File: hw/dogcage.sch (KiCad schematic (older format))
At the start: 23 parts, among them CON1 BARREL_JACK, P1 Door, P2 Lock, Q1 TIP120, Q2 TIP120, SW1 SW_PUSH, SW2 SW_PUSH, U1 LD1117S50TR, U2 ESP-01v090, U3 LD1117S33TR, U4 TEENSYLC

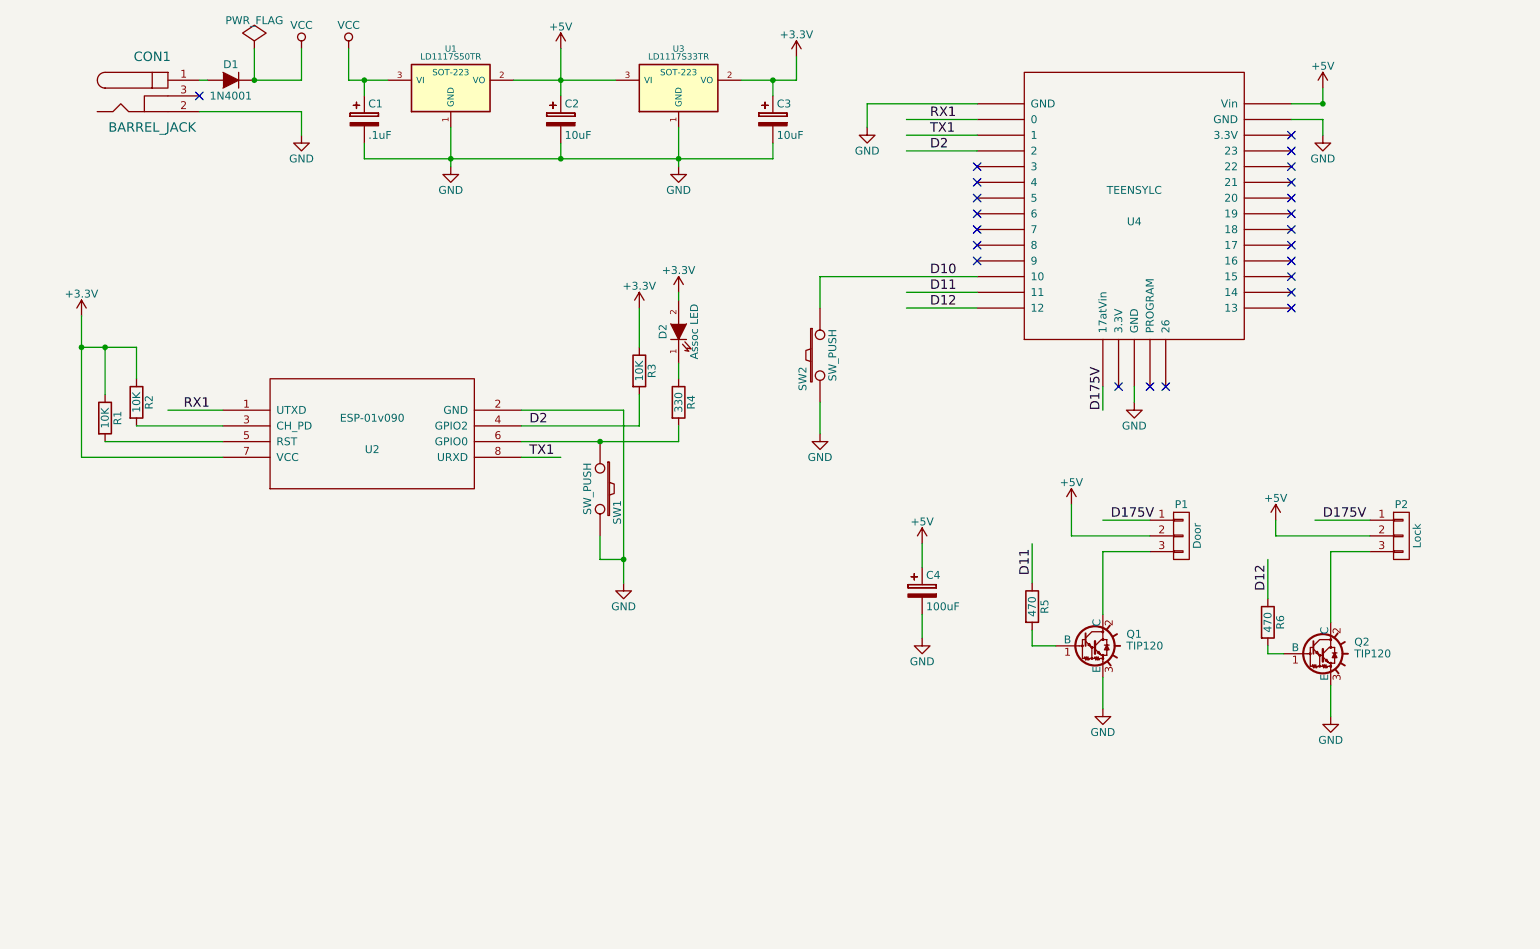
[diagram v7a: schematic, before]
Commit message: Added pwr_flag to GND, fixed DRC failures
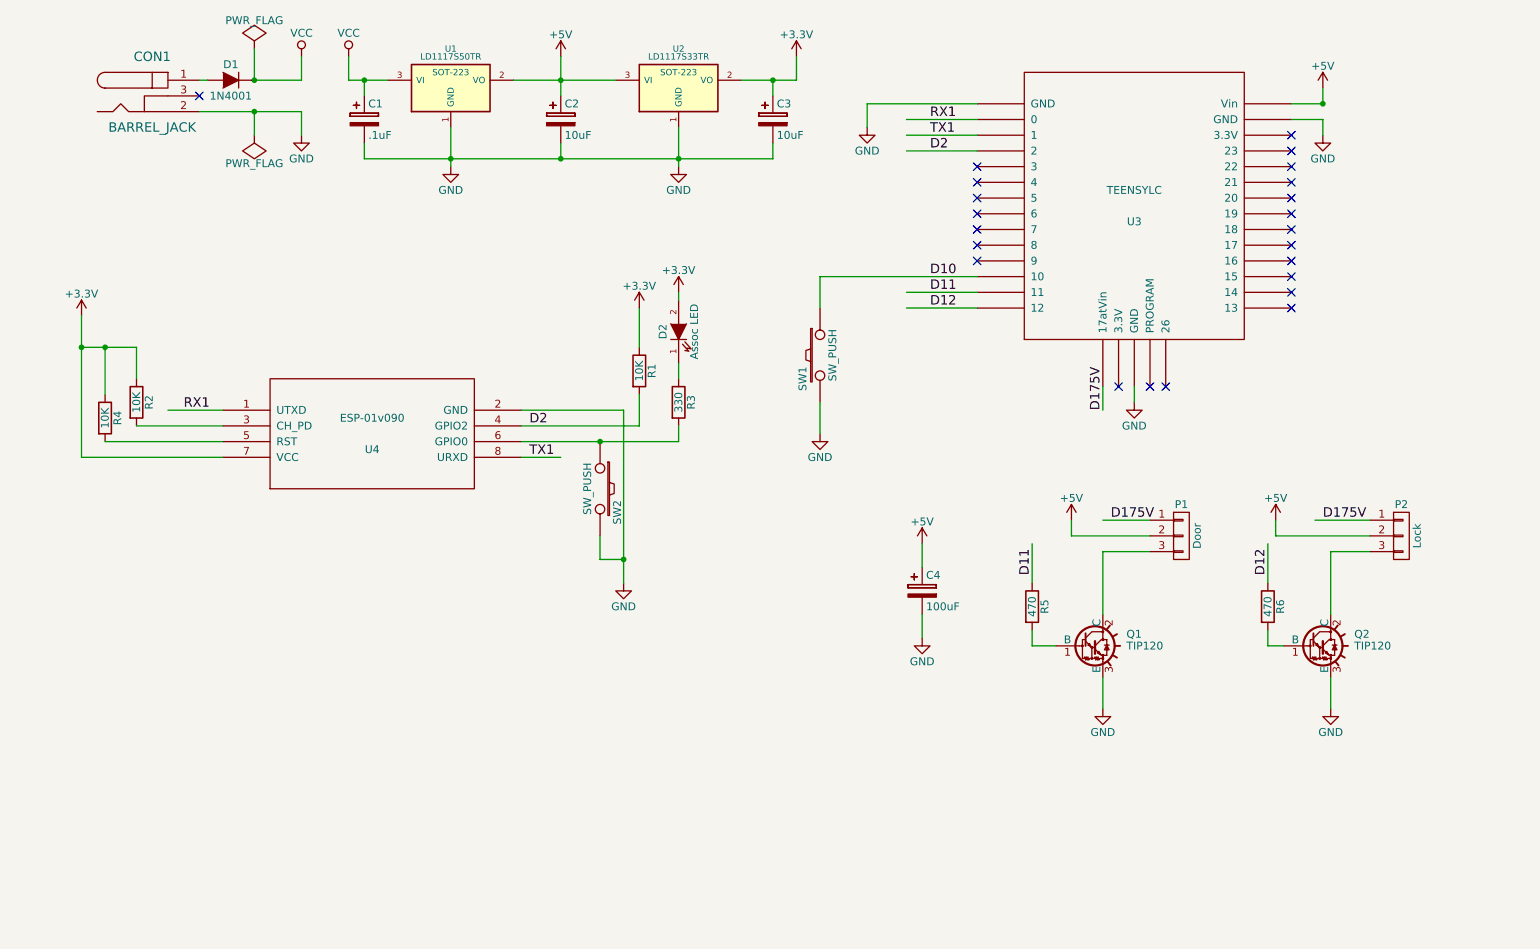
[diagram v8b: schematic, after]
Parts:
- renumbered R3 to R1, R4 to R3, R1 to R4, SW2 to SW1, SW1 to SW2, U3 to U2, U4 to U3, U2 to U4
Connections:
- wire segments 76 -> 77
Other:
- moved on the sheet: Q2, R6
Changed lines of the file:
@@
 $EndComp
 $Comp
-L TEENSYLC U4
+L TEENSYLC U3
 U 1 1 553C448F
 P 7650 1950
-F 0 "U4" H 7650 1850 50  0000 C CNN
+F 0 "U3" H 7650 1850 50  0000 C CNN
 F 1 "TEENSYLC" H 7650 2050 50  0000 C CNN
 F 2 "modules:Teensy-3.1" H 7650 1950 50  0001 C CNN
@@
 NoConn ~ 1700 1250
 $Comp
-L LD1117S33TR U3
+L LD1117S33TR U2
 U 1 1 553C5246
 P 4750 1200
-F 0 "U3" H 4750 1450 40  0000 C CNN
+F 0 "U2" H 4750 1450 40  0000 C CNN
 F 1 "LD1117S33TR" H 4750 1400 40  0000 C CNN
 F 2 "SOT-223" H 4750 1300 40  0000 C CNN
@@
 $EndComp
 $Comp
-L +5V #PWR09
-U 1 1 553C62D3
-P 4000 950
-F 0 "#PWR09" H 4000 800 50  0001 C CNN
-F 1 "+5V" H 4000 1090 50  0000 C CNN
-F 2 "" H 4000 950 60  0000 C CNN
-F 3 "" H 4000 950 60  0000 C CNN
-	1    4000 950
-	1    0    0    -1
-$EndComp
-$Comp
-L +3.3V #PWR010
+L +3.3V #PWR09
 U 1 1 553C6392
 P 5500 1000
-F 0 "#PWR010" H 5500 850 50  0001 C CNN
+F 0 "#PWR09" H 5500 850 50  0001 C CNN
 F 1 "+3.3V" H 5500 1140 50  0000 C CNN
 F 2 "" H 5500 1000 60  0000 C CNN
@@
 $EndComp
 $Comp
-L R R4
+L R R3
 U 1 1 553D19C7
 P 4750 3200
-F 0 "R4" V 4830 3200 50  0000 C CNN
+F 0 "R3" V 4830 3200 50  0000 C CNN
 F 1 "330" V 4750 3200 50  0000 C CNN
 F 2 "Resistors_ThroughHole:Resistor_Horizontal_RM10mm" V 4680 3200 30  0001 C CNN
@@
 $EndComp
 $Comp
-L SW_PUSH SW2
+L SW_PUSH SW1
 U 1 1 553C46F2
 P 5650 2900
-F 0 "SW2" H 5800 3010 50  0000 C CNN
+F 0 "SW1" H 5800 3010 50  0000 C CNN
 F 1 "SW_PUSH" H 5650 2820 50  0000 C CNN
 F 2 "Buttons_Switches_ThroughHole:SW_PUSH_SMALL" H 5650 2900 60  0001 C CNN
@@
 L TIP120 Q2
 U 1 1 559DEA4D
-P 8800 4800
-F 0 "Q2" H 9050 4875 50  0000 L CNN
-F 1 "TIP120" H 9050 4800 50  0000 L CNN
-F 2 "~" H 9050 4725 50  0000 L CIN
-F 3 "" H 8800 4800 50  0000 L CNN
-	1    8800 4800
+P 8800 4750
+F 0 "Q2" H 9050 4825 50  0000 L CNN
+F 1 "TIP120" H 9050 4750 50  0000 L CNN
+F 2 "~" H 9050 4675 50  0000 L CIN
+F 3 "" H 8800 4750 50  0000 L CNN
+	1    8800 4750
 	1    0    0    -1
 $EndComp
@@
 L R R6
 U 1 1 559DEC4E
-P 8500 4600
-F 0 "R6" V 8580 4600 50  0000 C CNN
-F 1 "470" V 8500 4600 50  0000 C CNN
-F 2 "" V 8430 4600 30  0000 C CNN
-F 3 "" H 8500 4600 30  0000 C CNN
-	1    8500 4600
-	1    0    0    -1
-$EndComp
-$Comp
-L GND #PWR011
+P 8500 4500
+F 0 "R6" V 8580 4500 50  0000 C CNN
+F 1 "470" V 8500 4500 50  0000 C CNN
+F 2 "" V 8430 4500 30  0000 C CNN
+F 3 "" H 8500 4500 30  0000 C CNN
+	1    8500 4500
+	1    0    0    -1
+$EndComp
+$Comp
+L GND #PWR010
 U 1 1 559DEE7F
-P 8900 5200
-F 0 "#PWR011" H 8900 4950 50  0001 C CNN
-F 1 "GND" H 8900 5050 50  0000 C CNN
-F 2 "" H 8900 5200 60  0000 C CNN
-F 3 "" H 8900 5200 60  0000 C CNN
-	1    8900 5200
+P 8900 5150
+F 0 "#PWR010" H 8900 4900 50  0001 C CNN
+F 1 "GND" H 8900 5000 50  0000 C CNN
+F 2 "" H 8900 5150 60  0000 C CNN
+F 3 "" H 8900 5150 60  0000 C CNN
+	1    8900 5150
 	1    0    0    -1
 $EndComp
@@
 $EndComp
 $Comp
-L GND #PWR012
+L GND #PWR011
 U 1 1 55A167AB
 P 3300 1700
-F 0 "#PWR012" H 3300 1450 50  0001 C CNN
+F 0 "#PWR011" H 3300 1450 50  0001 C CNN
 F 1 "GND" H 3300 1550 50  0000 C CNN
 F 2 "" H 3300 1700 60  0000 C CNN
@@
 $EndComp
 $Comp
+L VCC #PWR012
+U 1 1 55A16FD8
+P 2350 1000
+F 0 "#PWR012" H 2350 850 50  0001 C CNN
+F 1 "VCC" H 2350 1150 50  0000 C CNN
+F 2 "" H 2350 1000 60  0000 C CNN
+F 3 "" H 2350 1000 60  0000 C CNN
+	1    2350 1000
+	1    0    0    -1
+$EndComp
+$Comp
 L VCC #PWR013
-U 1 1 55A16FD8
-P 2350 950
-F 0 "#PWR013" H 2350 800 50  0001 C CNN
-F 1 "VCC" H 2350 1100 50  0000 C CNN
-F 2 "" H 2350 950 60  0000 C CNN
-F 3 "" H 2350 950 60  0000 C CNN
-	1    2350 950
-	1    0    0    -1
-$EndComp
-$Comp
-L VCC #PWR014
 U 1 1 55A17159
-P 2650 950
-F 0 "#PWR014" H 2650 800 50  0001 C CNN
-F 1 "VCC" H 2650 1100 50  0000 C CNN
-F 2 "" H 2650 950 60  0000 C CNN
-F 3 "" H 2650 950 60  0000 C CNN
-	1    2650 950
+P 2650 1000
+F 0 "#PWR013" H 2650 850 50  0001 C CNN
+F 1 "VCC" H 2650 1150 50  0000 C CNN
+F 2 "" H 2650 1000 60  0000 C CNN
+F 3 "" H 2650 1000 60  0000 C CNN
+	1    2650 1000
 	1    0    0    -1
 $EndComp
@@
 $EndComp
 $Comp
-L ESP-01v090 U2
+L ESP-01v090 U4
 U 1 1 55A18EAE
 P 2800 3400
-F 0 "U2" H 2800 3300 50  0000 C CNN
+F 0 "U4" H 2800 3300 50  0000 C CNN
 F 1 "ESP-01v090" H 2800 3500 50  0000 C CNN
 F 2 "" H 2800 3400 50  0001 C CNN
@@
 $EndComp
 $Comp
-L +3.3V #PWR015
+L +3.3V #PWR014
 U 1 1 55A19218
 P 950 2650
-F 0 "#PWR015" H 950 2500 50  0001 C CNN
+F 0 "#PWR014" H 950 2500 50  0001 C CNN
 F 1 "+3.3V" H 950 2790 50  0000 C CNN
 F 2 "" H 950 2650 60  0000 C CNN
@@
 $EndComp
 $Comp
-L GND #PWR016
+L GND #PWR015
 U 1 1 55A19378
 P 4400 4350
-F 0 "#PWR016" H 4400 4100 50  0001 C CNN
+F 0 "#PWR015" H 4400 4100 50  0001 C CNN
 F 1 "GND" H 4400 4200 50  0000 C CNN
 F 2 "" H 4400 4350 60  0000 C CNN
@@
 $EndComp
 $Comp
-L +3.3V #PWR017
+L +3.3V #PWR016
 U 1 1 55A1B48F
 P 4750 2500
-F 0 "#PWR017" H 4750 2350 50  0001 C CNN
+F 0 "#PWR016" H 4750 2350 50  0001 C CNN
 F 1 "+3.3V" H 4750 2640 50  0000 C CNN
 F 2 "" H 4750 2500 60  0000 C CNN
@@
 $EndComp
 $Comp
-L SW_PUSH SW1
+L SW_PUSH SW2
 U 1 1 55A19609
 P 4250 3750
-F 0 "SW1" H 4400 3860 50  0000 C CNN
+F 0 "SW2" H 4400 3860 50  0000 C CNN
 F 1 "SW_PUSH" H 4250 3670 50  0000 C CNN
 F 2 "" H 4250 3750 60  0000 C CNN
@@
 	1700 1150 1750 1150
 Wire Wire Line
-	2350 950  2350 1150
+	2350 1000 2350 1150
 Wire Wire Line
 	2350 1150 2050 1150
@@
 	7450 3100 7450 3250
 Wire Wire Line
-	2650 950  2650 1150
+	2650 1000 2650 1150
 Wire Wire Line
 	2650 1150 2900 1150
@@
 Connection ~ 2750 1150
 Wire Wire Line
-	4000 950  4000 1250
+	4000 1000 4000 1250
 Wire Wire Line
 	3700 1150 4350 1150
@@
 RX1
 $Comp
-L +3.3V #PWR018
+L +3.3V #PWR017
 U 1 1 55A898F1
 P 4500 2600
-F 0 "#PWR018" H 4500 2450 50  0001 C CNN
+F 0 "#PWR017" H 4500 2450 50  0001 C CNN
 F 1 "+3.3V" H 4500 2740 50  0000 C CNN
 F 2 "" H 4500 2600 60  0000 C CNN
@@
 	4500 2600 4500 2850
 $Comp
-L R R3
+L R R1
 U 1 1 55A89BD3
 P 4500 3000
-F 0 "R3" V 4580 3000 50  0000 C CNN
+F 0 "R1" V 4580 3000 50  0000 C CNN
 F 1 "10K" V 4500 3000 50  0000 C CNN
 F 2 "" V 4430 3000 30  0000 C CNN
@@
 $EndComp
 $Comp
-L R R1
+L R R4
 U 1 1 55A8A022
 P 1100 3300
-F 0 "R1" V 1180 3300 50  0000 C CNN
+F 0 "R4" V 1180 3300 50  0000 C CNN
 F 1 "10K" V 1100 3300 50  0000 C CNN
 F 2 "" V 1030 3300 30  0000 C CNN
@@
 Connection ~ 4250 3450
 $Comp
-L GND #PWR019
+L GND #PWR018
 U 1 1 55A8AFDE
 P 6300 4700
-F 0 "#PWR019" H 6300 4450 50  0001 C CNN
+F 0 "#PWR018" H 6300 4450 50  0001 C CNN
 F 1 "GND" H 6300 4550 50  0000 C CNN
 F 2 "" H 6300 4700 60  0000 C CNN
@@
 D2
 $Comp
-L GND #PWR020
+L GND #PWR019
 U 1 1 55A8B8EF
 P 7650 3200
-F 0 "#PWR020" H 7650 2950 50  0001 C CNN
+F 0 "#PWR019" H 7650 2950 50  0001 C CNN
 F 1 "GND" H 7650 3050 50  0000 C CNN
 F 2 "" H 7650 3200 60  0000 C CNN
@@
 $EndComp
 $Comp
-L GND #PWR021
+L GND #PWR020
 U 1 1 55A8B9CD
 P 8850 1500
-F 0 "#PWR021" H 8850 1250 50  0001 C CNN
+F 0 "#PWR020" H 8850 1250 50  0001 C CNN
 F 1 "GND" H 8850 1350 50  0000 C CNN
 F 2 "" H 8850 1500 60  0000 C CNN
@@
 D11
 Wire Wire Line
-	8500 4200 8500 4450
-Text Label 8500 4400 1    60   ~ 0
+	8500 4100 8500 4350
+Text Label 8500 4300 1    60   ~ 0
 D12
 NoConn ~ 6650 2100
@@
 NoConn ~ 6650 1700
 Wire Wire Line
-	8500 4750 8500 4800
-Wire Wire Line
-	8500 4800 8600 4800
+	8500 4650 8500 4750
+Wire Wire Line
+	8500 4750 8600 4750
 Wire Wire Line
 	3300 1450 3300 1700
@@
 	4250 4200 4400 4200
 Connection ~ 4400 4200
-Wire Wire Line
-	8900 5000 8900 5200
 Text Label 7450 3250 1    60   ~ 0
 D175V
@@
 NoConn ~ 8650 2600
 $Comp
-L +5V #PWR022
+L +5V #PWR021
 U 1 1 55A8E706
 P 8550 3950
-F 0 "#PWR022" H 8550 3800 50  0001 C CNN
+F 0 "#PWR021" H 8550 3800 50  0001 C CNN
 F 1 "+5V" H 8550 4090 50  0000 C CNN
 F 2 "" H 8550 3950 60  0000 C CNN
@@
 	8550 4050 9150 4050
 $Comp
-L +5V #PWR023
+L +5V #PWR022
 U 1 1 55A8E7E7
-P 7250 3850
-F 0 "#PWR023" H 7250 3700 50  0001 C CNN
-F 1 "+5V" H 7250 3990 50  0000 C CNN
-F 2 "" H 7250 3850 60  0000 C CNN
-F 3 "" H 7250 3850 60  0000 C CNN
-	1    7250 3850
-	1    0    0    -1
-$EndComp
-Wire Wire Line
-	7250 3850 7250 4050
+P 7250 3950
+F 0 "#PWR022" H 7250 3800 50  0001 C CNN
+F 1 "+5V" H 7250 4090 50  0000 C CNN
+F 2 "" H 7250 3950 60  0000 C CNN
+F 3 "" H 7250 3950 60  0000 C CNN
+	1    7250 3950
+	1    0    0    -1
+$EndComp
+Wire Wire Line
+	7250 3950 7250 4050
 Wire Wire Line
 	7250 4050 7750 4050
-Wire Wire Line
-	8900 4600 8900 4150
-Wire Wire Line
-	8900 4150 9150 4150
 Wire Wire Line
 	4750 1450 4750 1700
@@
 Wire Wire Line
 	5350 1650 5350 1550
+$Comp
+L +5V #PWR023
+U 1 1 55AB1974
+P 4000 1000
+F 0 "#PWR023" H 4000 850 50  0001 C CNN
+F 1 "+5V" H 4000 1140 50  0000 C CNN
+F 2 "" H 4000 1000 60  0000 C CNN
+F 3 "" H 4000 1000 60  0000 C CNN
+	1    4000 1000
+	1    0    0    -1
+$EndComp
+$Comp
+L PWR_FLAG #FLG024
+U 1 1 55AB1D8C
+P 2050 1500
+F 0 "#FLG024" H 2050 1595 50  0001 C CNN
+F 1 "PWR_FLAG" H 2050 1680 50  0000 C CNN
+F 2 "" H 2050 1500 60  0000 C CNN
+F 3 "" H 2050 1500 60  0000 C CNN
+	1    2050 1500
+	-1   0    0    1
+$EndComp
+Wire Wire Line
+	2050 1500 2050 1350
+Connection ~ 2050 1350
+Wire Wire Line
+	8900 4950 8900 5150
+Wire Wire Line
+	8900 4550 8900 4150
+Wire Wire Line
+	8900 4150 9150 4150
 $EndSCHEMATC
